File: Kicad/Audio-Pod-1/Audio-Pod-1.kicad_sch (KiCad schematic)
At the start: 24 parts, among them J1 Conn_01x04_Pin, J2 Conn_01x04_Socket, J3 USB_A Plug, SW1 SW_SPST, SW2 SW_SPST

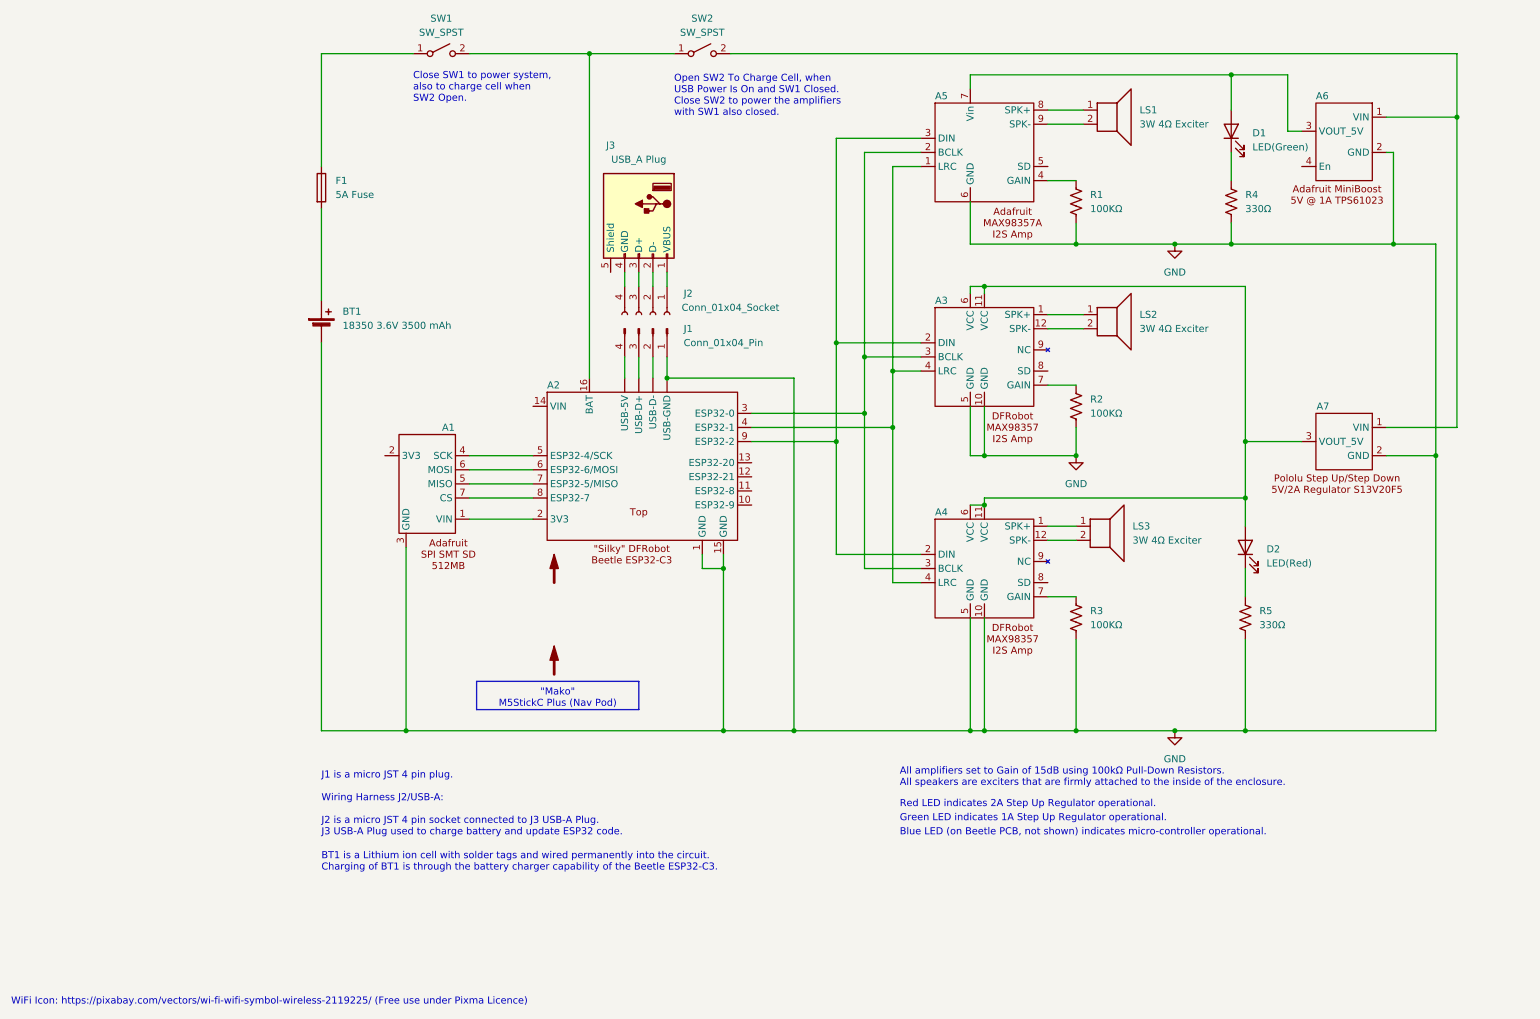
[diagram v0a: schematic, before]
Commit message: Added Audio Pod 1 and updated with images and tweaks other schematics.
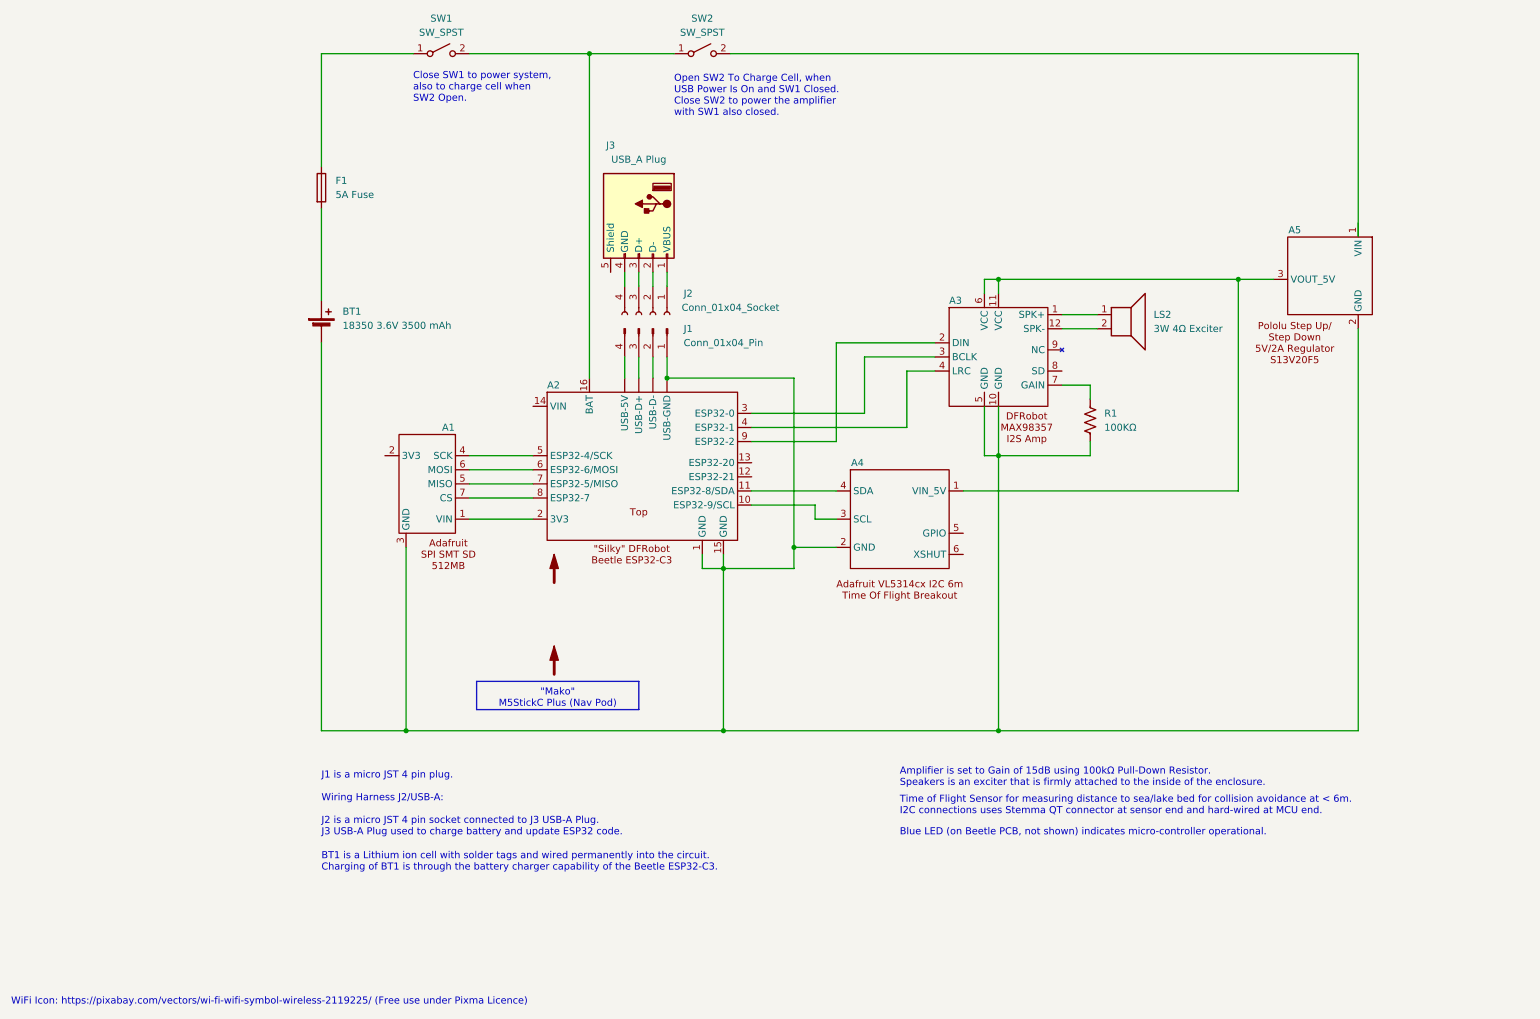
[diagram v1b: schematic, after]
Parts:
- removed A4: ~, symbol Audio-Pod-Symbols:DFRobot_MAX98357_I2S_Amplifier_Module
- removed A5: ~, symbol Audio-Pod-Symbols:Adafruit_MAX98357A_I2S_Amplifier_Module
- removed A6: ~, symbol Audio-Pod-Symbols:Adafruiit_MiniBoost_5V_1A_TPS61023
- removed D1: LED(Green), symbol Device:LED
- removed D2: LED(Red), symbol Device:LED
- removed LS1, LS3: 3W 4Ω Exciter, symbol Device:Speaker
- removed R2, R3: 100KΩ, symbol Device:R_US
- removed R4, R5: 330Ω, symbol Device:R_US
- added A4: ~, symbol Audio-Pod-Symbols:Adafruit_VL53L4CX_I2C_ToF_Breakout
- renumbered A7 to A5
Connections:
- net at R1.1: now also A3.7 (GAIN)
- net at A3.11 (VCC), A3.6 (VCC), A5.3 (VOUT_5V): now also A4.1 (VIN_5V)
- net at SW2.2 (B): no longer A5.1 (VIN)
- net at A2.10 (ESP32-9/SCL): now also A4.3 (SCL)
- net at A2.11 (ESP32-8/SDA): now also A4.4 (SDA)
- net GND: no longer names the net of A1.3 (GND), A2. (USB-GND), A2.1 (GND), A2.15 (GND), A3.10 (GND), A3.5 (GND), A5.2 (GND), BT1.2 (-), J1.1 (Pin_1), R1.2
- net GND: now also A4.2 (GND)
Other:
- note added: "Amplifier is set to Gain of 15dB using 100kΩ Pull-Down Resistor. Speakers is an exciter that is firmly attached to the inside of the enclosure."
- note added: "Open SW2 To Charge Cell, when USB Power Is On and SW1 Closed. Close SW2 to power the amplifier with SW1 also closed."
- note added: "Time of Flight Sensor for measuring distance to sea/lake bed for collision avoidance at < 6m. I2C connections uses Stemma QT connector at sensor end and hard-wired at MCU end."
- note removed: "All amplifiers set to Gain of 15dB using 100kΩ Pull-Down Resistors. All speakers are exciters that are firmly attached to the inside of the enclosure."
- note removed: "Green LED indicates 1A Step Up Regulator operational."
- note removed: "Open SW2 To Charge Cell, when USB Power Is On and SW1 Closed. Close SW2 to power the amplifiers with SW1 also closed."
- note removed: "Red LED indicates 2A Step Up Regulator operational."
- title: Mercator Origins Audio Pod 2 -> Mercator Origins Audio Pod 1
- moved on the sheet: A3, LS2
